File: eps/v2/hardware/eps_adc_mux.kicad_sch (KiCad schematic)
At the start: 38 parts, among them U4 ADS124S08

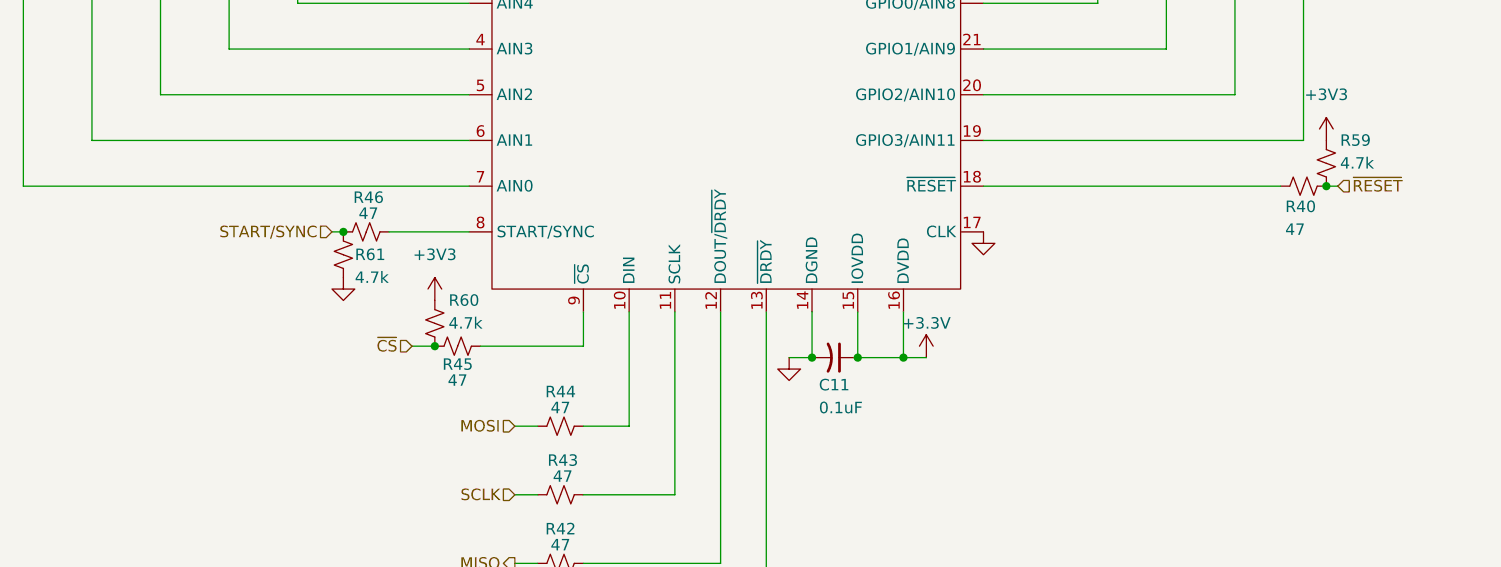
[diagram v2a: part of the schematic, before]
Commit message: Pull up/down fixes
-moved series termination resistors before the pull up/downs
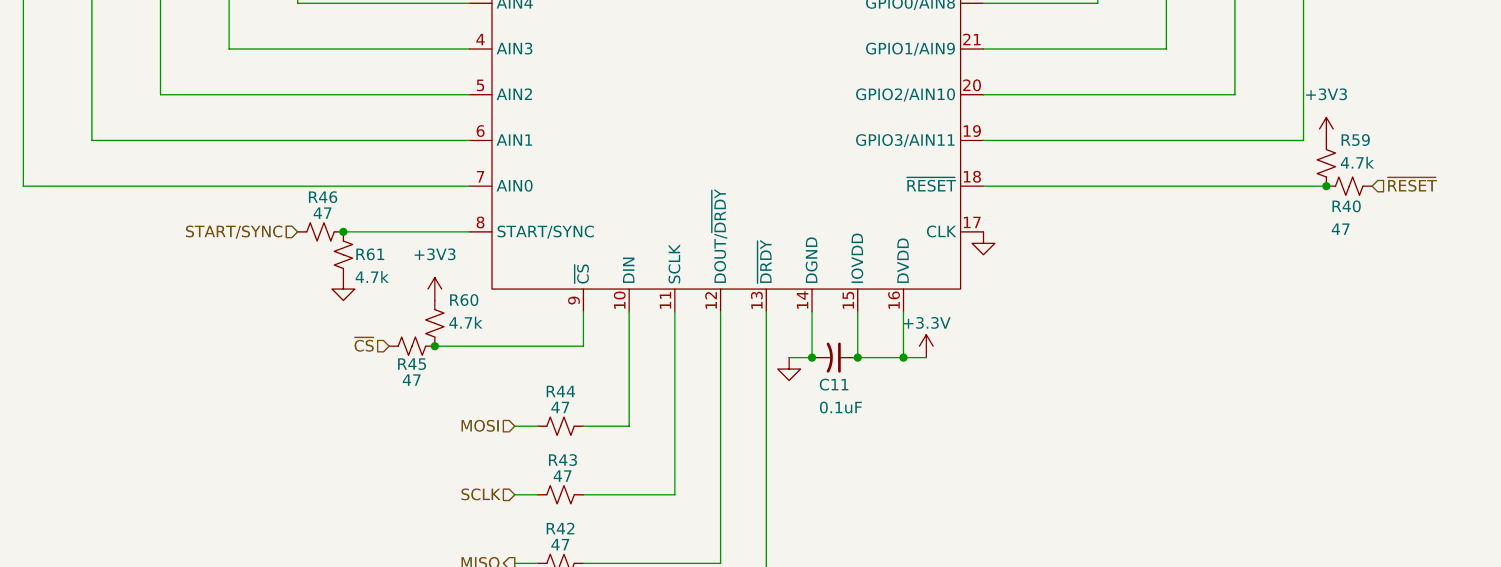
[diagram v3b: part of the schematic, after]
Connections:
- net START/SYNC: no longer R61.1
- net ~{CS}: no longer R60.2
- net ~{RESET}: no longer R59.2
- net at R45.2, U4.9 (~{CS}): now also R60.2
- net at R40.2, U4.18 (~{RESET}): now also R59.2
- net at R46.1, U4.8 (START/SYNC): now also R61.1
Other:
- moved on the sheet: R40, R45, R46
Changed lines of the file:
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@@
 	)
 	(junction
-		(at 101.6 100.33)
-		(diameter 0)
-		(color 0 0 0 0)
-	)
-	(junction
-		(at 210.82 95.25)
+		(at 111.76 113.03)
 		(diameter 0)
 		(color 0 0 0 0)
@@
 	)
 	(junction
+		(at 210.82 95.25)
+		(diameter 0)
+		(color 0 0 0 0)
+	)
+	(junction
 		(at 185.42 64.77)
 		(diameter 0)
@@
 	)
 	(junction
-		(at 111.76 113.03)
+		(at 101.6 100.33)
 		(diameter 0)
 		(color 0 0 0 0)
@@
 	(wire
 		(pts
-			(xy 116.84 113.03) (xy 128.27 113.03)
-		)
-		(stroke
-			(width 0)
-			(type default)
-		)
-	)
-	(wire
-		(pts
 			(xy 185.42 74.93) (xy 185.42 64.77)
 		)
@@
 	(wire
 		(pts
-			(xy 106.68 100.33) (xy 115.57 100.33)
-		)
-		(stroke
-			(width 0)
-			(type default)
-		)
-	)
-	(wire
-		(pts
 			(xy 128.27 57.15) (xy 121.92 57.15)
 		)
@@
 	(wire
 		(pts
-			(xy 100.33 100.33) (xy 101.6 100.33)
-		)
-		(stroke
-			(width 0)
-			(type default)
-		)
-	)
-	(wire
-		(pts
 			(xy 123.19 137.16) (xy 120.65 137.16)
 		)
@@
 	(wire
 		(pts
-			(xy 109.22 113.03) (xy 111.76 113.03)
-		)
-		(stroke
-			(width 0)
-			(type default)
-		)
-	)
-	(wire
-		(pts
 			(xy 115.57 80.01) (xy 88.9 80.01)
 		)
@@
 	(wire
 		(pts
+			(xy 172.72 95.25) (xy 210.82 95.25)
+		)
+		(stroke
+			(width 0)
+			(type default)
+		)
+	)
+	(wire
+		(pts
 			(xy 96.52 62.23) (xy 96.52 74.93)
 		)
@@
 	(wire
 		(pts
-			(xy 210.82 95.25) (xy 212.09 95.25)
+			(xy 111.76 113.03) (xy 128.27 113.03)
 		)
 		(stroke
@@
 	(wire
 		(pts
-			(xy 81.28 85.09) (xy 81.28 62.23)
+			(xy 101.6 100.33) (xy 115.57 100.33)
 		)
 		(stroke
@@
 	(wire
 		(pts
-			(xy 128.27 113.03) (xy 128.27 109.22)
+			(xy 81.28 85.09) (xy 81.28 62.23)
 		)
 		(stroke
@@
 	(wire
 		(pts
-			(xy 66.04 95.25) (xy 66.04 62.23)
+			(xy 128.27 113.03) (xy 128.27 109.22)
 		)
 		(stroke
@@
 	(wire
 		(pts
-			(xy 138.43 52.07) (xy 138.43 57.15)
+			(xy 66.04 95.25) (xy 66.04 62.23)
 		)
 		(stroke
@@
 	(wire
 		(pts
-			(xy 172.72 64.77) (xy 175.26 64.77)
+			(xy 138.43 52.07) (xy 138.43 57.15)
 		)
 		(stroke
@@
 	(wire
 		(pts
-			(xy 104.14 69.85) (xy 104.14 62.23)
+			(xy 172.72 64.77) (xy 175.26 64.77)
 		)
 		(stroke
@@
 	(wire
 		(pts
-			(xy 123.19 121.92) (xy 120.65 121.92)
+			(xy 104.14 69.85) (xy 104.14 62.23)
 		)
 		(stroke
@@
 	(wire
 		(pts
-			(xy 205.74 95.25) (xy 172.72 95.25)
+			(xy 123.19 121.92) (xy 120.65 121.92)
 		)
 		(stroke
@@
 	(hierarchical_label "START{slash}SYNC"
 		(shape input)
-		(at 100.33 100.33 180)
+		(at 96.52 100.33 180)
 		(effects
 			(font
@@
 	(hierarchical_label "~{RESET}"
 		(shape input)
-		(at 212.09 95.25 0)
+		(at 215.9 95.25 0)
 		(effects
 			(font
@@
 	(hierarchical_label "~{CS}"
 		(shape input)
-		(at 109.22 113.03 180)
+		(at 106.68 113.03 180)
 		(effects
 			(font
@@
 	(symbol
 		(lib_id "Device:R_Small_US")
-		(at 114.3 113.03 90)
+		(at 109.22 113.03 90)
 		(unit 1)
 		(body_style 1)
@@
 		(dnp no)
 		(property "Reference" "R45"
-			(at 114.3 115.062 90)
+			(at 109.22 115.062 90)
 			(show_name no)
 			(do_not_autoplace no)
@@
 		)
 		(property "Value" "47"
-			(at 114.3 116.84 90)
+			(at 109.22 116.84 90)
 			(show_name no)
 			(do_not_autoplace no)
@@
 		)
 		(property "Footprint" ""
-			(at 114.3 113.03 0)
+			(at 109.22 113.03 0)
 			(hide yes)
 			(show_name no)
@@
 		)
 		(property "Datasheet" ""
-			(at 114.3 113.03 0)
+			(at 109.22 113.03 0)
 			(hide yes)
 			(show_name no)
@@
 		)
 		(property "Description" "Resistor, small US symbol"
-			(at 114.3 113.03 0)
+			(at 109.22 113.03 0)
 			(hide yes)
 			(show_name no)
@@
 	(symbol
 		(lib_id "Device:R_Small_US")
-		(at 208.28 95.25 270)
+		(at 213.36 95.25 270)
 		(unit 1)
 		(body_style 1)
@@
 		(dnp no)
 		(property "Reference" "R40"
-			(at 206.248 97.536 90)
+			(at 211.328 97.536 90)
 			(show_name no)
 			(do_not_autoplace no)
@@
 		)
 		(property "Value" "47"
-			(at 206.248 100.076 90)
+			(at 211.328 100.076 90)
 			(show_name no)
 			(do_not_autoplace no)
@@
 		)
 		(property "Footprint" ""
-			(at 208.28 95.25 0)
+			(at 213.36 95.25 0)
 			(hide yes)
 			(show_name no)
@@
 		)
 		(property "Datasheet" ""
-			(at 208.28 95.25 0)
+			(at 213.36 95.25 0)
 			(hide yes)
 			(show_name no)
@@
 		)
 		(property "Description" "Resistor, small US symbol"
-			(at 208.28 95.25 0)
+			(at 213.36 95.25 0)
 			(hide yes)
 			(show_name no)
@@
 	(symbol
 		(lib_id "Device:R_Small_US")
-		(at 104.14 100.33 270)
+		(at 99.06 100.33 270)
 		(unit 1)
 		(body_style 1)
@@
 		(dnp no)
 		(property "Reference" "R46"
-			(at 104.394 96.52 90)
+			(at 99.314 96.52 90)
 			(show_name no)
 			(do_not_autoplace no)
@@
 		)
 		(property "Value" "47"
-			(at 104.394 98.298 90)
+			(at 99.314 98.298 90)
 			(show_name no)
 			(do_not_autoplace no)
@@
 		)
 		(property "Footprint" ""
-			(at 104.14 100.33 0)
+			(at 99.06 100.33 0)
 			(hide yes)
 			(show_name no)
@@
 		)
 		(property "Datasheet" ""
-			(at 104.14 100.33 0)
+			(at 99.06 100.33 0)
 			(hide yes)
 			(show_name no)
@@
 		)
 		(property "Description" "Resistor, small US symbol"
-			(at 104.14 100.33 0)
+			(at 99.06 100.33 0)
 			(hide yes)
 			(show_name no)
